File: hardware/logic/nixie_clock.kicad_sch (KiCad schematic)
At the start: 0 parts

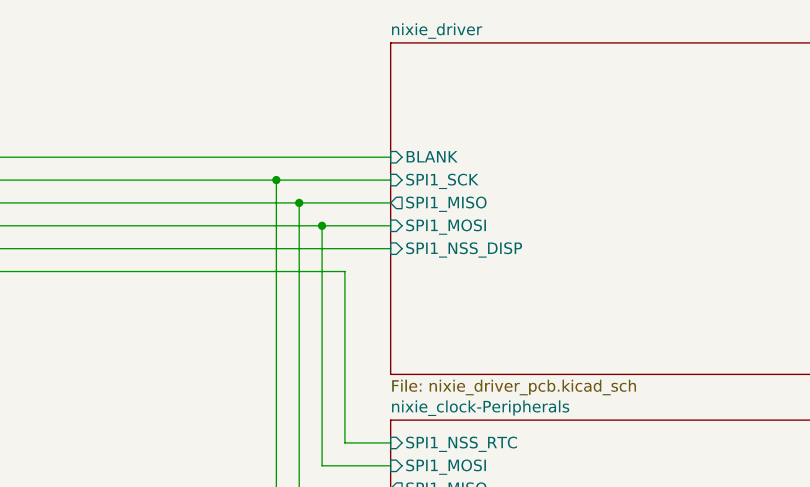
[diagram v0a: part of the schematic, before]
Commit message: Changed connectors to driver board, fixed oscillator connections
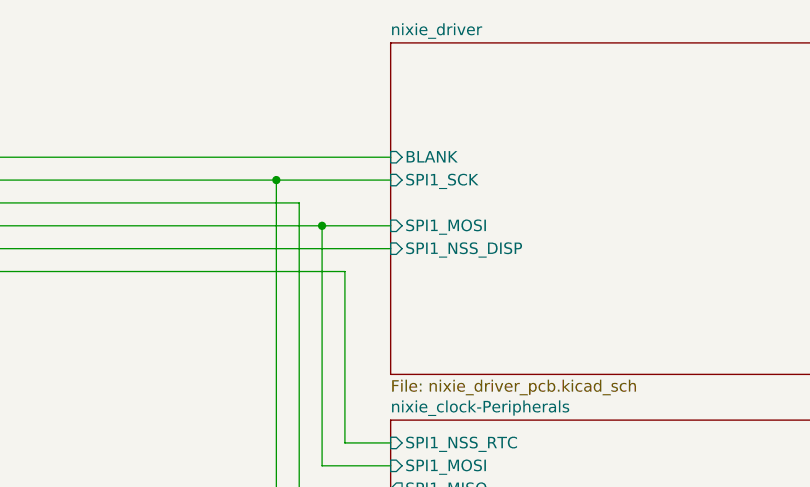
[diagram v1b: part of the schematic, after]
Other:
- sheet nixie_driver ports: added none; removed SPI1_MISO
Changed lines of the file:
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@@
 (kicad_sch (version 20230121) (generator eeschema)
   (paper "A4")
-  (junction (at 137.16 36.83) (diameter 0) (color 0 0 0 0)
-  )
   (junction (at 134.62 34.29) (diameter 0) (color 0 0 0 0)
   )
@@
   )
   (wire (pts (xy 77.47 81.28) (xy 147.32 81.28))
-    (stroke (width 0) (type default))
-  )
-  (wire (pts (xy 137.16 36.83) (xy 147.32 36.83))
     (stroke (width 0) (type default))
   )
@@
       (effects (font (size 1.27 1.27)) (justify left))
     )
-    (pin "SPI1_MISO" output (at 147.32 36.83 180)
-      (effects (font (size 1.27 1.27)) (justify left))
-    )
